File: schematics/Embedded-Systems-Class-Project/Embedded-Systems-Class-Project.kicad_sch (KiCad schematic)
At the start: 2 parts

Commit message: lcd and i2c converter schematic
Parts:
- added U?: LCD_16X2, symbol New_Library:LCD_16X2
- added U?: I2C_LCM1602, symbol New_Library:I2C_LCM1602
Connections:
- new net: U?.1 (VSS), U?.1 (VSS)
- new net: U?.10 (D3), U?.10 (D3)
- new net: U?.11 (D4), U?.11 (D4)
- new net: U?.12 (D5), U?.12 (D5)
- new net: U?.13 (D6), U?.13 (D6)
- new net: U?.14 (D7), U?.14 (D7)
- new net: U?.15 (A), U?.15 (LEDA)
- new net: U?.16 (K), U?.16 (LEDK)
- new net: U?.2 (VDD), U?.2 (VDD)
- new net: U?.3 (VEE), U?.3 (Vo)
- new net: U?.4 (RS), U?.4 (RS)
- new net: U?.5 (RW), U?.5 (RW)
- new net: U?.6 (E), U?.6 (E)
- new net: U?.7 (D0), U?.7 (D0)
- new net: U?.8 (D1), U?.8 (D1)
- new net: U?.9 (D2), U?.9 (D2)
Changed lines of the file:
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@@
 (kicad_sch (version 20211123) (generator eeschema)
   (paper "A4")
+  (wire (pts (xy 243.84 35.56) (xy 245.11 35.56))
+    (stroke (width 0) (type default) (color 0 0 0 0))
+  )
+  (wire (pts (xy 243.84 63.5) (xy 245.11 63.5))
+    (stroke (width 0) (type default) (color 0 0 0 0))
+  )
+  (wire (pts (xy 243.84 53.34) (xy 245.11 53.34))
+    (stroke (width 0) (type default) (color 0 0 0 0))
+  )
+  (wire (pts (xy 243.84 48.26) (xy 245.11 48.26))
+    (stroke (width 0) (type default) (color 0 0 0 0))
+  )
+  (wire (pts (xy 243.84 40.64) (xy 245.11 40.64))
+    (stroke (width 0) (type default) (color 0 0 0 0))
+  )
+  (wire (pts (xy 243.84 50.8) (xy 245.11 50.8))
+    (stroke (width 0) (type default) (color 0 0 0 0))
+  )
+  (wire (pts (xy 243.84 55.88) (xy 245.11 55.88))
+    (stroke (width 0) (type default) (color 0 0 0 0))
+  )
+  (wire (pts (xy 243.84 60.96) (xy 245.11 60.96))
+    (stroke (width 0) (type default) (color 0 0 0 0))
+  )
+  (wire (pts (xy 243.84 71.12) (xy 245.11 71.12))
+    (stroke (width 0) (type default) (color 0 0 0 0))
+  )
+  (wire (pts (xy 243.84 58.42) (xy 245.11 58.42))
+    (stroke (width 0) (type default) (color 0 0 0 0))
+  )
+  (wire (pts (xy 243.84 68.58) (xy 245.11 68.58))
+    (stroke (width 0) (type default) (color 0 0 0 0))
+  )
+  (wire (pts (xy 243.84 33.02) (xy 245.11 33.02))
+    (stroke (width 0) (type default) (color 0 0 0 0))
+  )
+  (wire (pts (xy 243.84 45.72) (xy 245.11 45.72))
+    (stroke (width 0) (type default) (color 0 0 0 0))
+  )
+  (wire (pts (xy 243.84 66.04) (xy 245.11 66.04))
+    (stroke (width 0) (type default) (color 0 0 0 0))
+  )
+  (wire (pts (xy 243.84 38.1) (xy 245.11 38.1))
+    (stroke (width 0) (type default) (color 0 0 0 0))
+  )
+  (wire (pts (xy 243.84 43.18) (xy 245.11 43.18))
+    (stroke (width 0) (type default) (color 0 0 0 0))
+  )
   (symbol (lib_id "Device:Thermocouple") (at 64.77 59.69 0) (unit 1)
     (in_bom yes) (on_board yes) (fields_autoplaced)
@@
     (pin "1")
     (pin "2")
+  )
+  (symbol (lib_id "New_Library:LCD_16X2") (at 254 29.21 0) (unit 1)
+    (in_bom yes) (on_board yes) (fields_autoplaced)
+    (property "Reference" "U?" (id 0) (at 264.16 50.7999 0)
+      (effects (font (size 1.27 1.27)) (justify left))
+    )
+    (property "Value" "LCD_16X2" (id 1) (at 264.16 53.3399 0)
+      (effects (font (size 1.27 1.27)) (justify left))
+    )
+    (property "Footprint" "" (id 2) (at 257.81 29.21 0)
+      (effects (font (size 1.27 1.27)) hide)
+    )
+    (property "Datasheet" "" (id 3) (at 257.81 29.21 0)
+      (effects (font (size 1.27 1.27)) hide)
+    )
+    (pin "1")
+    (pin "10")
+    (pin "11")
+    (pin "12")
+    (pin "13")
+    (pin "14")
+    (pin "15")
+    (pin "16")
+    (pin "2")
+    (pin "3")
+    (pin "4")
+    (pin "5")
+    (pin "6")
+    (pin "7")
+    (pin "8")
+    (pin "9")
   )
   (symbol (lib_id "Sensor_Temperature:MAX31855KASA") (at 77.47 59.69 0) (unit 1)
@@
     (pin "7")
   )
+  (symbol (lib_id "New_Library:I2C_LCM1602") (at 232.41 30.48 0) (unit 1)
+    (in_bom yes) (on_board yes) (fields_autoplaced)
+    (property "Reference" "U?" (id 0) (at 233.68 26.67 0))
+    (property "Value" "I2C_LCM1602" (id 1) (at 233.68 29.21 0))
+    (property "Footprint" "" (id 2) (at 232.41 30.48 0)
+      (effects (font (size 1.27 1.27)) hide)
+    )
+    (property "Datasheet" "" (id 3) (at 232.41 30.48 0)
+      (effects (font (size 1.27 1.27)) hide)
+    )
+    (pin "")
+    (pin "")
+    (pin "")
+    (pin "")
+    (pin "")
+    (pin "")
+    (pin "")
+    (pin "1")
+    (pin "10")
+    (pin "11")
+    (pin "12")
+    (pin "13")
+    (pin "14")
+    (pin "15")
+    (pin "16")
+    (pin "2")
+    (pin "3")
+    (pin "4")
+    (pin "5")
+    (pin "6")
+    (pin "7")
+    (pin "8")
+    (pin "9")
+  )
   (sheet_instances
     (path "/" (page "1"))
@@
       (reference "TC?") (unit 1) (value "Thermocouple") (footprint "")
     )
+    (path "/67b32d2d-4b4e-4212-b97d-46de8b5ce173"
+      (reference "U?") (unit 1) (value "LCD_16X2") (footprint "")
+    )
     (path "/a7737520-3a3a-4c82-8c7a-5d4c51d46684"
       (reference "U?") (unit 1) (value "MAX31855KASA") (footprint "Package_SO:SOIC-8_3.9x4.9mm_P1.27mm")
     )
+    (path "/e53559b4-ecc3-46d1-a3ba-c30c1f78eb69"
+      (reference "U?") (unit 1) (value "I2C_LCM1602") (footprint "")
+    )
   )

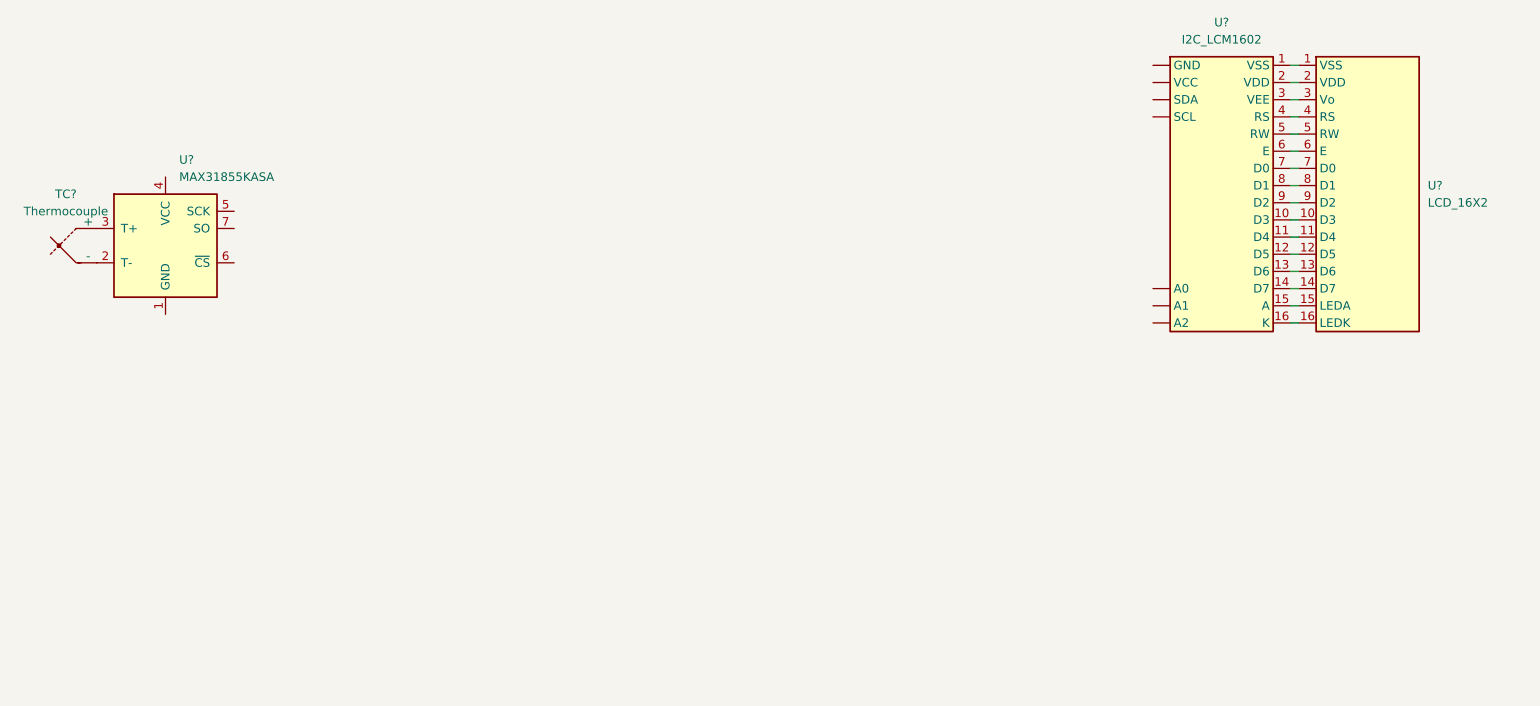
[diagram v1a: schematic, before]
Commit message: updated schematic with micro sd card model
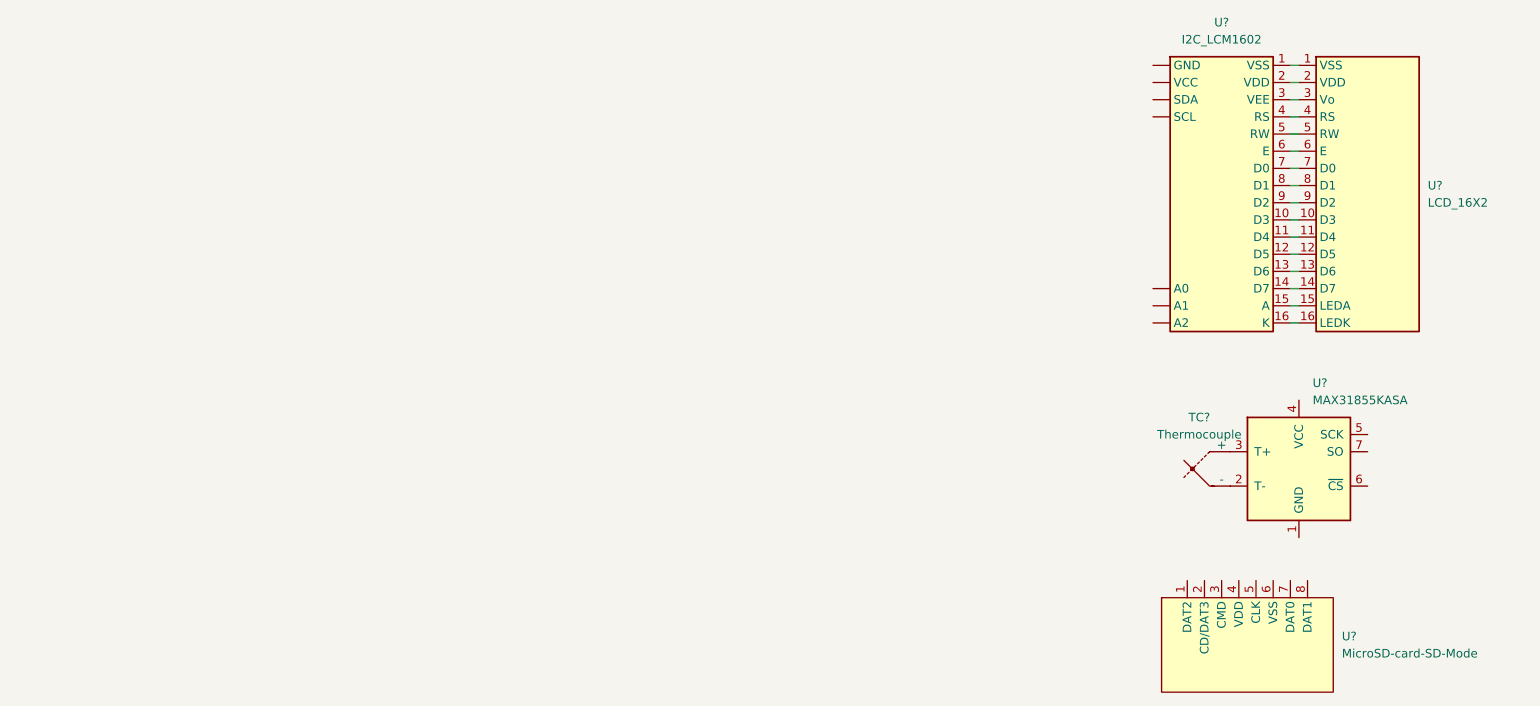
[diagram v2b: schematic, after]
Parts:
- added U?: MicroSD-card-SD-Mode, symbol Embedded-Systems-Class-Project:MicroSD-card-SD-Mode
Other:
- moved on the sheet: TC?, U?
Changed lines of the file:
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@@
     (stroke (width 0) (type default) (color 0 0 0 0))
   )
-  (symbol (lib_id "Device:Thermocouple") (at 64.77 59.69 0) (unit 1)
+  (symbol (lib_id "Device:Thermocouple") (at 232.41 92.71 0) (unit 1)
     (in_bom yes) (on_board yes) (fields_autoplaced)
-    (property "Reference" "TC?" (id 0) (at 62.738 52.07 0))
-    (property "Value" "Thermocouple" (id 1) (at 62.738 54.61 0))
-    (property "Footprint" "" (id 2) (at 50.165 58.42 0)
+    (property "Reference" "TC?" (id 0) (at 230.378 85.09 0))
+    (property "Value" "Thermocouple" (id 1) (at 230.378 87.63 0))
+    (property "Footprint" "" (id 2) (at 217.805 91.44 0)
       (effects (font (size 1.27 1.27)) hide)
     )
-    (property "Datasheet" "~" (id 3) (at 50.165 58.42 0)
+    (property "Datasheet" "~" (id 3) (at 217.805 91.44 0)
       (effects (font (size 1.27 1.27)) hide)
     )
@@
     (pin "9")
   )
-  (symbol (lib_id "Sensor_Temperature:MAX31855KASA") (at 77.47 59.69 0) (unit 1)
+  (symbol (lib_id "Sensor_Temperature:MAX31855KASA") (at 245.11 92.71 0) (unit 1)
     (in_bom yes) (on_board yes) (fields_autoplaced)
-    (property "Reference" "U?" (id 0) (at 79.4894 46.99 0)
+    (property "Reference" "U?" (id 0) (at 247.1294 80.01 0)
       (effects (font (size 1.27 1.27)) (justify left))
     )
-    (property "Value" "MAX31855KASA" (id 1) (at 79.4894 49.53 0)
+    (property "Value" "MAX31855KASA" (id 1) (at 247.1294 82.55 0)
       (effects (font (size 1.27 1.27)) (justify left))
     )
-    (property "Footprint" "Package_SO:SOIC-8_3.9x4.9mm_P1.27mm" (id 2) (at 102.87 68.58 0)
+    (property "Footprint" "Package_SO:SOIC-8_3.9x4.9mm_P1.27mm" (id 2) (at 270.51 101.6 0)
       (effects (font (size 1.27 1.27) italic) hide)
     )
-    (property "Datasheet" "http://datasheets.maximintegrated.com/en/ds/MAX31855.pdf" (id 3) (at 77.47 59.69 0)
+    (property "Datasheet" "http://datasheets.maximintegrated.com/en/ds/MAX31855.pdf" (id 3) (at 245.11 92.71 0)
       (effects (font (size 1.27 1.27)) hide)
     )
@@
     (pin "6")
     (pin "7")
+  )
+  (symbol (lib_id "Embedded-Systems-Class-Project:MicroSD-card-SD-Mode") (at 237.49 115.57 0) (unit 1)
+    (in_bom yes) (on_board yes) (fields_autoplaced)
+    (property "Reference" "U?" (id 0) (at 251.46 117.4749 0)
+      (effects (font (size 1.27 1.27)) (justify left))
+    )
+    (property "Value" "MicroSD-card-SD-Mode" (id 1) (at 251.46 120.0149 0)
+      (effects (font (size 1.27 1.27)) (justify left))
+    )
+    (property "Footprint" "" (id 2) (at 236.22 114.3 0)
+      (effects (font (size 1.27 1.27)) hide)
+    )
+    (property "Datasheet" "" (id 3) (at 236.22 114.3 0)
+      (effects (font (size 1.27 1.27)) hide)
+    )
+    (pin "1")
+    (pin "2")
+    (pin "3")
+    (pin "4")
+    (pin "5")
+    (pin "6")
+    (pin "7")
+    (pin "8")
   )
   (symbol (lib_id "New_Library:I2C_LCM1602") (at 232.41 30.48 0) (unit 1)
@@
       (reference "U?") (unit 1) (value "MAX31855KASA") (footprint "Package_SO:SOIC-8_3.9x4.9mm_P1.27mm")
     )
+    (path "/e2b677ce-76aa-4483-8231-a9168f66cf77"
+      (reference "U?") (unit 1) (value "MicroSD-card-SD-Mode") (footprint "")
+    )
     (path "/e53559b4-ecc3-46d1-a3ba-c30c1f78eb69"

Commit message: Revert "Dodanie do schematu karty mikroSD"
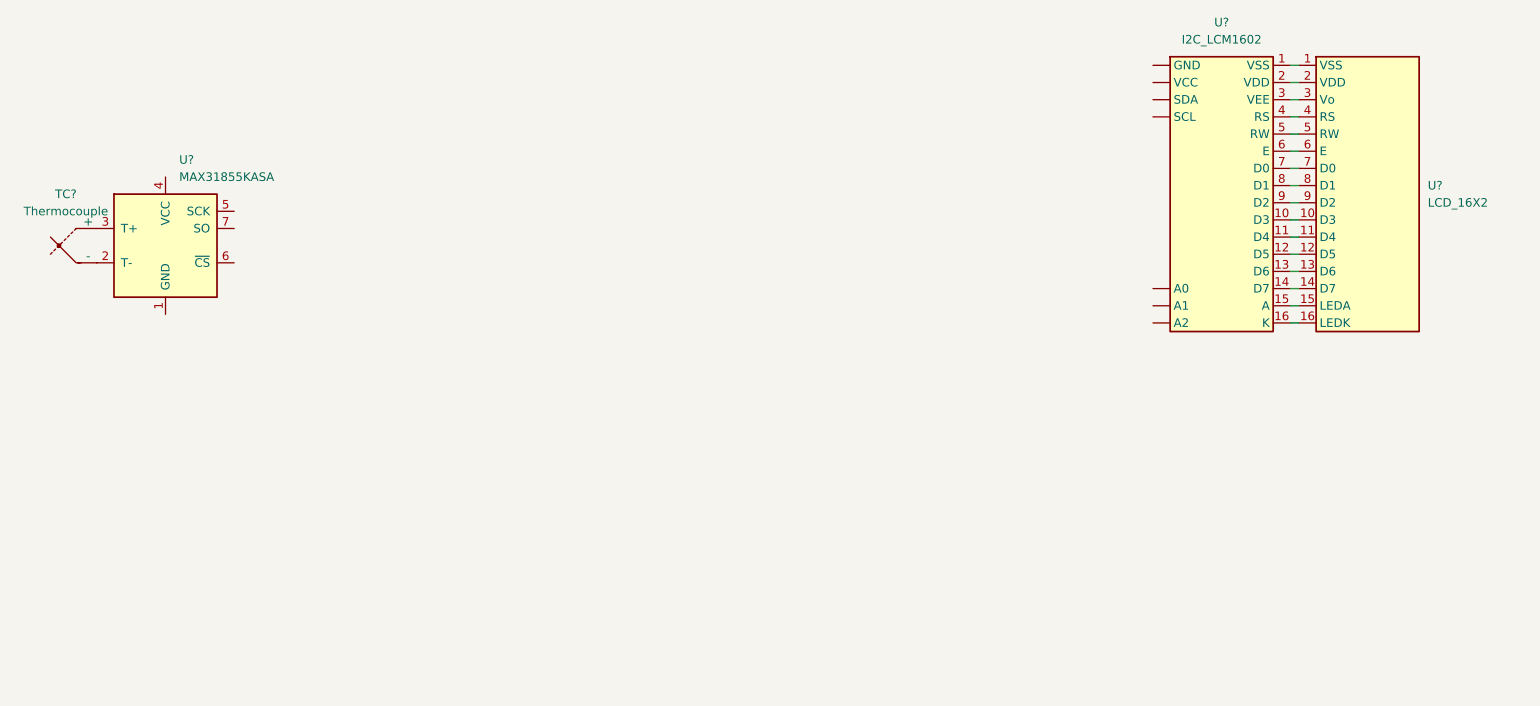
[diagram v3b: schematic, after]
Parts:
- removed U?: MicroSD-card-SD-Mode, symbol Embedded-Systems-Class-Project:MicroSD-card-SD-Mode
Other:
- moved on the sheet: TC?, U?
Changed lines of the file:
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@@
     (stroke (width 0) (type default) (color 0 0 0 0))
   )
-  (symbol (lib_id "Device:Thermocouple") (at 232.41 92.71 0) (unit 1)
+  (symbol (lib_id "Device:Thermocouple") (at 64.77 59.69 0) (unit 1)
     (in_bom yes) (on_board yes) (fields_autoplaced)
-    (property "Reference" "TC?" (id 0) (at 230.378 85.09 0))
-    (property "Value" "Thermocouple" (id 1) (at 230.378 87.63 0))
-    (property "Footprint" "" (id 2) (at 217.805 91.44 0)
+    (property "Reference" "TC?" (id 0) (at 62.738 52.07 0))
+    (property "Value" "Thermocouple" (id 1) (at 62.738 54.61 0))
+    (property "Footprint" "" (id 2) (at 50.165 58.42 0)
       (effects (font (size 1.27 1.27)) hide)
     )
-    (property "Datasheet" "~" (id 3) (at 217.805 91.44 0)
+    (property "Datasheet" "~" (id 3) (at 50.165 58.42 0)
       (effects (font (size 1.27 1.27)) hide)
     )
@@
     (pin "9")
   )
-  (symbol (lib_id "Sensor_Temperature:MAX31855KASA") (at 245.11 92.71 0) (unit 1)
+  (symbol (lib_id "Sensor_Temperature:MAX31855KASA") (at 77.47 59.69 0) (unit 1)
     (in_bom yes) (on_board yes) (fields_autoplaced)
-    (property "Reference" "U?" (id 0) (at 247.1294 80.01 0)
+    (property "Reference" "U?" (id 0) (at 79.4894 46.99 0)
       (effects (font (size 1.27 1.27)) (justify left))
     )
-    (property "Value" "MAX31855KASA" (id 1) (at 247.1294 82.55 0)
+    (property "Value" "MAX31855KASA" (id 1) (at 79.4894 49.53 0)
       (effects (font (size 1.27 1.27)) (justify left))
     )
-    (property "Footprint" "Package_SO:SOIC-8_3.9x4.9mm_P1.27mm" (id 2) (at 270.51 101.6 0)
+    (property "Footprint" "Package_SO:SOIC-8_3.9x4.9mm_P1.27mm" (id 2) (at 102.87 68.58 0)
       (effects (font (size 1.27 1.27) italic) hide)
     )
-    (property "Datasheet" "http://datasheets.maximintegrated.com/en/ds/MAX31855.pdf" (id 3) (at 245.11 92.71 0)
+    (property "Datasheet" "http://datasheets.maximintegrated.com/en/ds/MAX31855.pdf" (id 3) (at 77.47 59.69 0)
       (effects (font (size 1.27 1.27)) hide)
     )
@@
     (pin "6")
     (pin "7")
-  )
-  (symbol (lib_id "Embedded-Systems-Class-Project:MicroSD-card-SD-Mode") (at 237.49 115.57 0) (unit 1)
-    (in_bom yes) (on_board yes) (fields_autoplaced)
-    (property "Reference" "U?" (id 0) (at 251.46 117.4749 0)
-      (effects (font (size 1.27 1.27)) (justify left))
-    )
-    (property "Value" "MicroSD-card-SD-Mode" (id 1) (at 251.46 120.0149 0)
-      (effects (font (size 1.27 1.27)) (justify left))
-    )
-    (property "Footprint" "" (id 2) (at 236.22 114.3 0)
-      (effects (font (size 1.27 1.27)) hide)
-    )
-    (property "Datasheet" "" (id 3) (at 236.22 114.3 0)
-      (effects (font (size 1.27 1.27)) hide)
-    )
-    (pin "1")
-    (pin "2")
-    (pin "3")
-    (pin "4")
-    (pin "5")
-    (pin "6")
-    (pin "7")
-    (pin "8")
   )
   (symbol (lib_id "New_Library:I2C_LCM1602") (at 232.41 30.48 0) (unit 1)
@@
       (reference "U?") (unit 1) (value "MAX31855KASA") (footprint "Package_SO:SOIC-8_3.9x4.9mm_P1.27mm")
     )
-    (path "/e2b677ce-76aa-4483-8231-a9168f66cf77"
-      (reference "U?") (unit 1) (value "MicroSD-card-SD-Mode") (footprint "")
-    )
     (path "/e53559b4-ecc3-46d1-a3ba-c30c1f78eb69"
